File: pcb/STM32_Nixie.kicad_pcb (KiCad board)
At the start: 2 copper layers, 134 parts, among them J1 CONN_USBC_RCPT_USB2.0_USB4085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, J1 CON_SAMTEC_14P_2R_1m27_P_KEY_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, J2 CONN_USBC_RCPT_USB2.0_USB4085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, Q1 NFET_250V_10A_TPH1110FNH,L1Q, SW1 ENC_SPST_24PPR_PEC12R-4225F-S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, U1 IC_HV5622PG-G, U2 IC_HV5622PG-G, U3 IC_MCU_STM32F100C4T6B_48LQFP, U4 IC_LVL_MC14504BDTR2G, U5 REG_SW_BOOST_TI_TLV61046ADBV, U6 REG_SW_BOOST_TI_LM51561HPWPR, U7 REG_LDO_3V3_250mA_TI_LP5907MF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, U8 IC_FTDI_FT231XS, X1 XTAL_8M_20PPM_18pF_ECS-80-18-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, X2 XTAL_32K768_10PPM_7pF_ECS-.32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

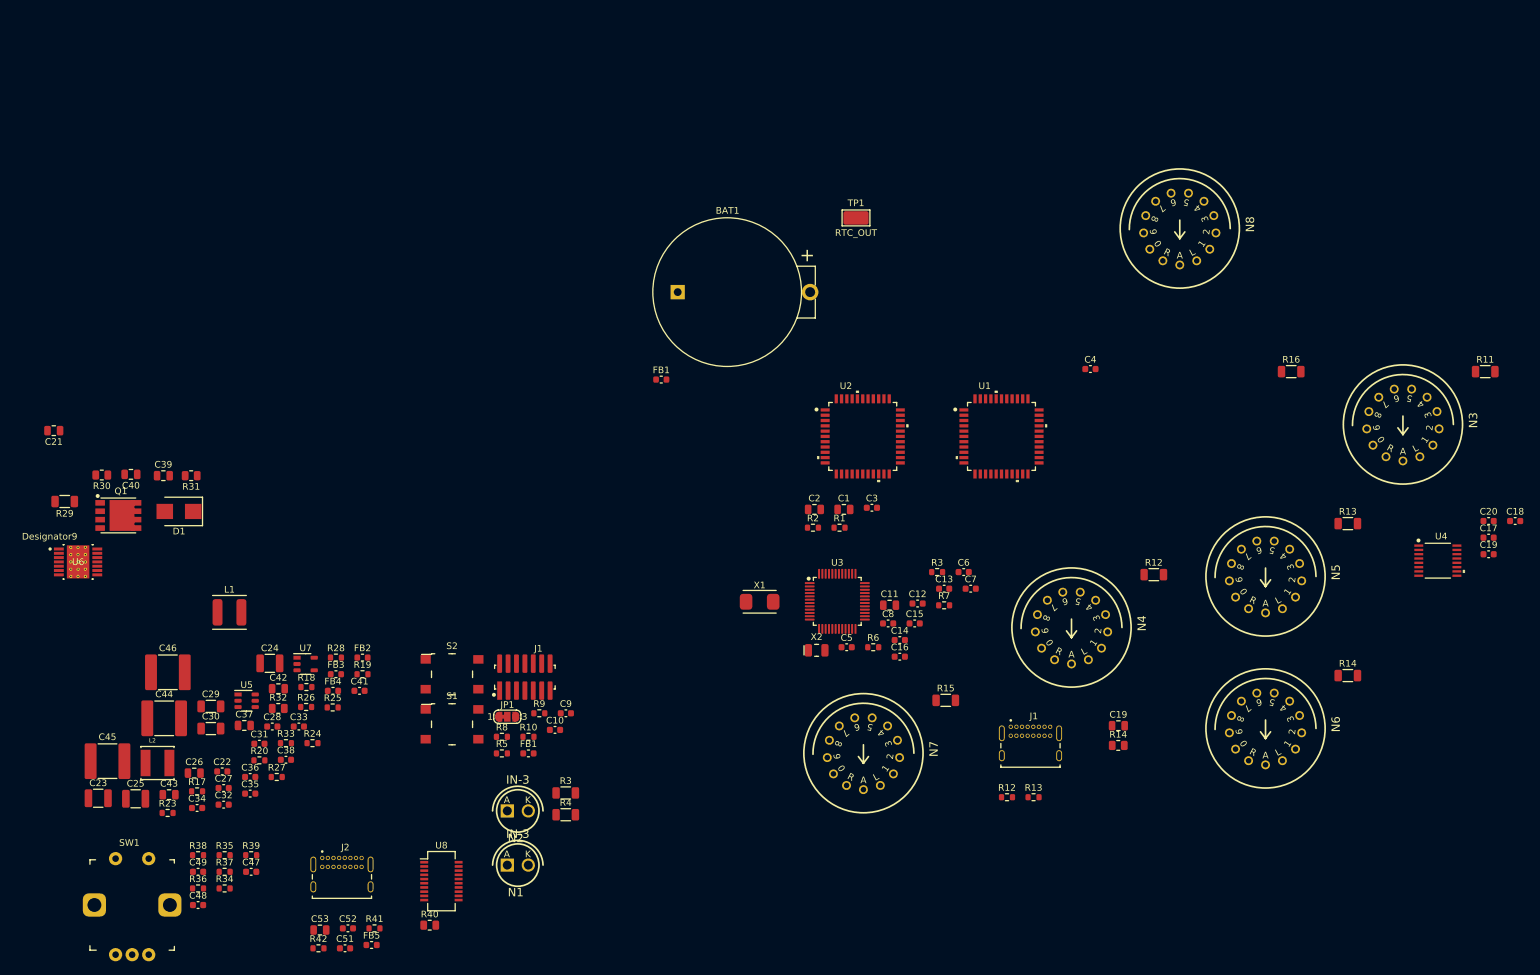
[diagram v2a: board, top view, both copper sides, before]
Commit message: Fixed a bunch of footprints and added missing 3D models
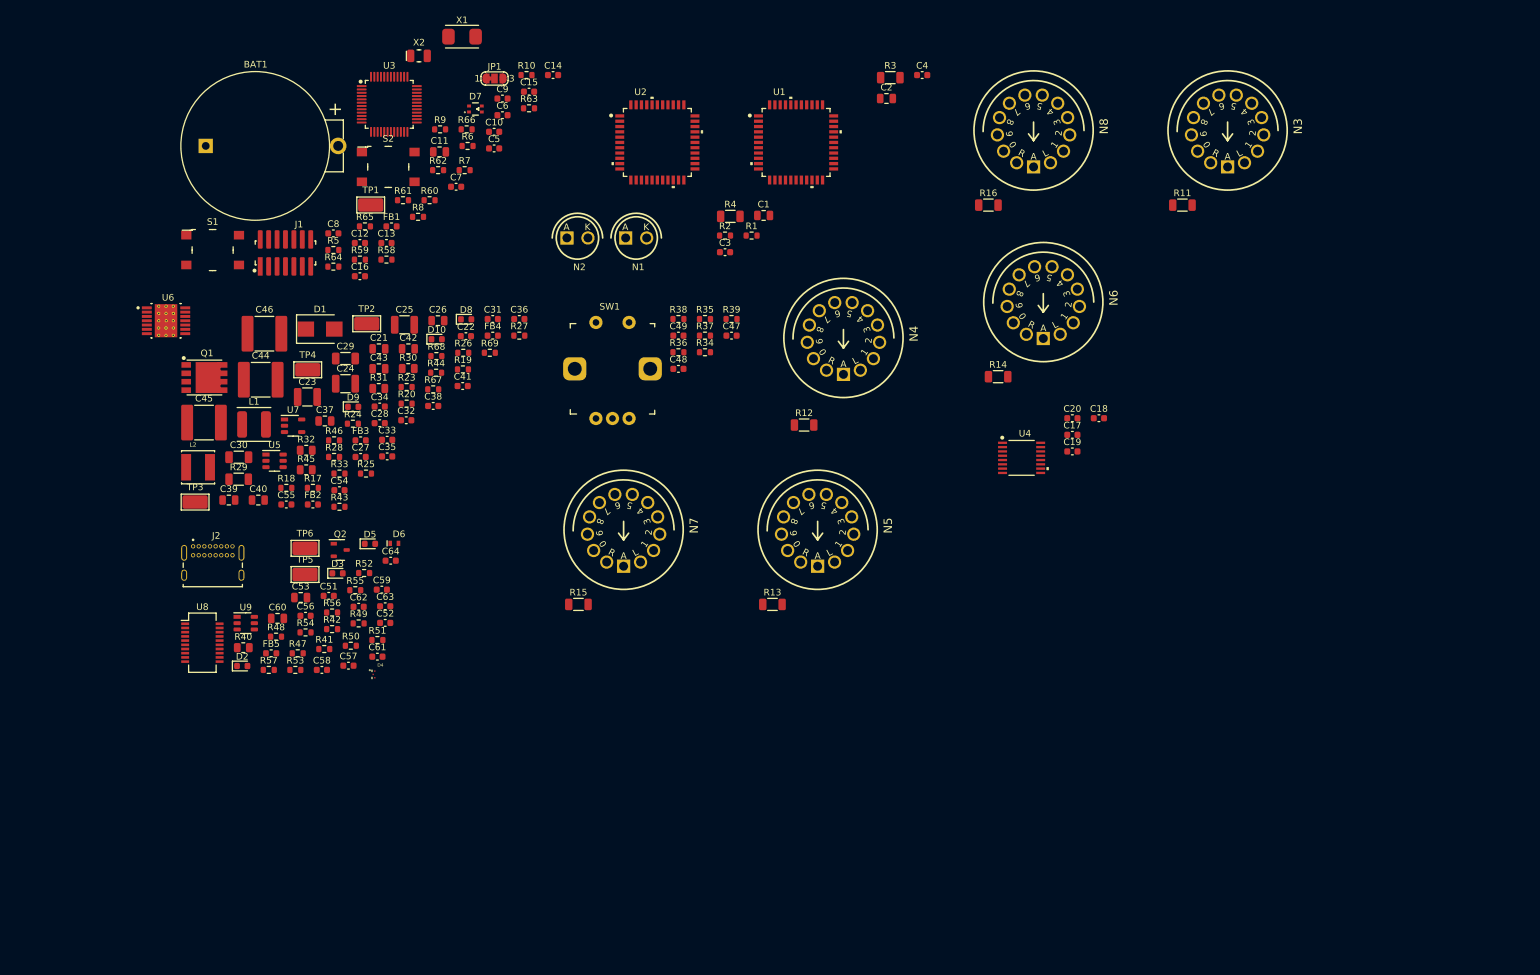
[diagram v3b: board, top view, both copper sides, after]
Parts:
- removed the C19 at (233.3, 95.4)
- removed the C19 at (177.4, 121.3)
- removed the FB1 at (108.4, 69.0)
- removed the FB1 at (88.3, 125.4)
- removed the J1 at (164.1, 125.8)
- removed the J1 at (87.8, 113.9)
- removed the R12 at (160.6, 132.1)
- removed the R12 at (182.8, 98.4)
- removed the R13 at (164.6, 132.1)
- removed the R13 at (212.1, 90.7)
- removed the R14 at (212.1, 113.7)
- removed the R14 at (177.4, 124.2)
- removed the R3 at (94.0, 131.4)
- removed the R3 at (150.0, 98.1)
- added C19: CAP_CER_0u1_50V_X7R_0603, Capacitor_SMD:C_0603_1608Metric, F.Cu at (170.5, 79.8)
- added C54: CAP_CER_0u1_50V_X7R_0603, Capacitor_SMD:C_0603_1608Metric, F.Cu at (59.8, 85.7)
- added C55: CAP_CER_0u1_50V_X7R_0603, Capacitor_SMD:C_0603_1608Metric, F.Cu at (51.8, 87.8)
- added C56: CAP_CER_47p_50V_NP0_0603, Capacitor_SMD:C_0603_1608Metric, F.Cu at (54.7, 104.7)
- added C57: CAP_CER_47p_50V_NP0_0603, Capacitor_SMD:C_0603_1608Metric, F.Cu at (61.1, 112.2)
- added C58: CAP_CER_0u1_50V_X7R_0603, Capacitor_SMD:C_0603_1608Metric, F.Cu at (57.1, 112.8)
- added C59: CAP_CER_0u1_50V_X7R_0603, Capacitor_SMD:C_0603_1608Metric, F.Cu at (66.2, 100.7)
- added C60: CAP_CER_4u7_16V_X7R_0805, Capacitor_SMD:C_0805_2012Metric, F.Cu at (50.4, 105.0)
- added C61: CAP_CER_0u1_50V_X7R_0603, Capacitor_SMD:C_0603_1608Metric, F.Cu at (65.5, 110.8)
- added C62: CAP_CER_0u1_50V_X7R_0603, Capacitor_SMD:C_0603_1608Metric, F.Cu at (62.7, 103.3)
- added C63: CAP_CER_0u1_50V_X7R_0603, Capacitor_SMD:C_0603_1608Metric, F.Cu at (66.7, 103.2)
- added C64: CAP_CER_0u1_50V_X7R_0603, Capacitor_SMD:C_0603_1608Metric, F.Cu at (67.5, 96.3)
- added D10: LED_GREEN_0603, LED_SMD:LED_0603_1608Metric, F.Cu at (74.5, 62.9)
- added D2: LED_AMBER_0603, LED_SMD:LED_0603_1608Metric, F.Cu at (45.1, 112.2)
- added D3: LED_GREEN_0603, LED_SMD:LED_0603_1608Metric, F.Cu at (59.5, 98.2)
- added D4: D_TVS_BI_3V6_20W_3-XFDFN, arjun_footprints:DIO_ESD122DMYR, F.Cu at (65.0, 113.5)
- added D5: LED_RED_0603, LED_SMD:LED_0603_1608Metric, F.Cu at (64.4, 93.8)
- added D6: D_TVS_UNI_5V_700W_2-UDFN, arjun_footprints:QFN-2L_STM, F.Cu at (68.1, 93.7)
- added D7: LED_RGB_0606, arjun_footprints:EAST1616RGBB2_EVE, F.Cu at (80.3, 28.1)
- added D8: LED_AMBER_0603, LED_SMD:LED_0603_1608Metric, F.Cu at (78.9, 59.9)
- added D9: LED_GREEN_0603, LED_SMD:LED_0603_1608Metric, F.Cu at (61.9, 73.1)
- added FB1: FER_1K_0A6_0603, Inductor_SMD:L_0603_1608Metric, F.Cu at (67.6, 45.9)
- added J1: CON_SAMTEC_14P_2R_1m27_P_KEY_FTSH-107-01-L-DV-K-TR, arjun_footprints:CON_FTSH-107-01-x-DV-K, F.Cu at (51.6, 49.9)
- added Q2: NFET_60V_0A5_2N7002KT1G, arjun_footprints:SOT-23_ONSEMI, F.Cu at (59.9, 94.7)
- added R12: RES_17K4_1P_1/4W_1206, Resistor_SMD:R_1206_3216Metric, F.Cu at (130.0, 75.8)
- added R13: RES_17K4_1P_1/4W_1206, Resistor_SMD:R_1206_3216Metric, F.Cu at (125.2, 102.9)
- added R14: RES_17K4_1P_1/4W_1206, Resistor_SMD:R_1206_3216Metric, F.Cu at (159.3, 68.5)
- added R3: RES_150K_1P_1/4W_1206, Resistor_SMD:R_1206_3216Metric, F.Cu at (143.0, 23.4)
- added R43: RES_33K_1P_1/10W_0603, Resistor_SMD:R_0603_1608Metric, F.Cu at (59.8, 88.2)
- added R44: RES_4K7_1P_1/10W_0603, Resistor_SMD:R_0603_1608Metric, F.Cu at (74.4, 68.0)
- added R45: RES_499K_1P_1/4W_0805, Resistor_SMD:R_0805_2012Metric, F.Cu at (54.8, 82.6)
- added R46: RES_4K7_1P_1/10W_0603, Resistor_SMD:R_0603_1608Metric, F.Cu at (59.0, 78.2)
- added R47: RES_27R_1P_1/10W_0603, Resistor_SMD:R_0603_1608Metric, F.Cu at (53.5, 110.3)
- added R48: RES_27R_1P_1/10W_0603, Resistor_SMD:R_0603_1608Metric, F.Cu at (50.2, 107.8)
- added R49: RES_10K_1P_1/10W_0603, Resistor_SMD:R_0603_1608Metric, F.Cu at (62.7, 105.8)
- added R50: RES_1K5_1P_1/10W_0603, Resistor_SMD:R_0603_1608Metric, F.Cu at (61.5, 109.2)
- added R51: RES_698R_1P_1/10W_0603, Resistor_SMD:R_0603_1608Metric, F.Cu at (65.5, 108.3)
- added R52: RES_DNP_0603, Resistor_SMD:R_0603_1608Metric, F.Cu at (63.5, 98.2)
- added R53: RES_10K_1P_1/10W_0603, Resistor_SMD:R_0603_1608Metric, F.Cu at (53.1, 112.8)
- added R54: RES_232K_1P_1/10W_0603, Resistor_SMD:R_0603_1608Metric, F.Cu at (54.7, 107.2)
- added R55: RES_26K1_1P_1/10W_0603, Resistor_SMD:R_0603_1608Metric, F.Cu at (62.2, 100.8)
- added R56: RES_10K_1P_1/10W_0603, Resistor_SMD:R_0603_1608Metric, F.Cu at (58.7, 104.2)
- added R57: RES_3K3_1P_1/10W_0603, Resistor_SMD:R_0603_1608Metric, F.Cu at (49.1, 112.8)
- added R58: RES_499R_1P_1/10W_0603, Resistor_SMD:R_0603_1608Metric, F.Cu at (66.9, 50.9)
- added R59: RES_1K5_1P_1/10W_0603, Resistor_SMD:R_0603_1608Metric, F.Cu at (62.9, 50.9)
- added R60: RES_698R_1P_1/10W_0603, Resistor_SMD:R_0603_1608Metric, F.Cu at (73.4, 41.9)
- added R61: RES_10K_1P_1/10W_0603, Resistor_SMD:R_0603_1608Metric, F.Cu at (69.4, 41.9)
- added R62: RES_10K_1P_1/10W_0603, Resistor_SMD:R_0603_1608Metric, F.Cu at (74.7, 37.4)
- added R63: RES_10K_1P_1/10W_0603, Resistor_SMD:R_0603_1608Metric, F.Cu at (88.4, 28.0)
- added R64: RES_30R_1P_1/10W_0603, Resistor_SMD:R_0603_1608Metric, F.Cu at (58.9, 51.9)
- added R65: RES_30R_1P_1/10W_0603, Resistor_SMD:R_0603_1608Metric, F.Cu at (63.6, 45.9)
- added R66: RES_30R_1P_1/10W_0603, Resistor_SMD:R_0603_1608Metric, F.Cu at (79.0, 31.2)
- added R67: RES_1K5_1P_1/10W_0603, Resistor_SMD:R_0603_1608Metric, F.Cu at (73.9, 70.5)
- added R68: RES_9K31_1P_1/10W_0603, Resistor_SMD:R_0603_1608Metric, F.Cu at (74.4, 65.4)
- added R69: RES_698R_1P_1/10W_0603, Resistor_SMD:R_0603_1608Metric, F.Cu at (82.5, 64.9)
- added TP2: TP_KEYSTONE_5019, arjun_footprints:TestPoint_Keystone_5019_Minature, F.Cu at (63.9, 60.6)
- added TP3: TP_KEYSTONE_5019, arjun_footprints:TestPoint_Keystone_5019_Minature, F.Cu at (38.0, 87.5)
- added TP4: TP_KEYSTONE_5019, arjun_footprints:TestPoint_Keystone_5019_Minature, F.Cu at (55.0, 67.5)
- added TP5: TP_KEYSTONE_5019, arjun_footprints:TestPoint_Keystone_5019_Minature, F.Cu at (54.6, 98.4)
- added TP6: TP_KEYSTONE_5019, arjun_footprints:TestPoint_Keystone_5019_Minature, F.Cu at (54.6, 94.5)
- added U9: IC_LSW_TI_TPS2552D, arjun_footprints:SOT-23-6_TI, F.Cu at (45.6, 105.8)
- N1, N2: value IN-3 -> Val**
- N3, N4, N5, N6, N7, N8: value IN-14 -> Val**
- U1, U2: value IC_HV5622PG-G -> IC_SR_MC_HV5622PG-G
- U4: value IC_LVL_MC14504BDTR2G -> IC_LVL_ONSEMI_MC14504BDTR2G
- moved R34 108.7 mm to (115.0, 64.9)
- moved R36 108.7 mm to (111.0, 64.9)
- moved SW1 108.7 mm to (95.3, 67.4)
- moved C47 108.7 mm to (119.0, 62.4)
- moved C48 108.7 mm to (111.0, 67.4)
- moved C49 108.7 mm to (111.0, 62.4)
- moved R35 108.7 mm to (115.0, 59.8)
- moved R37 108.7 mm to (115.0, 62.4)
- moved R38 108.7 mm to (111.0, 59.8)
- moved R39 108.7 mm to (119.0, 59.8)
- moved X2 108.0 mm to (71.8, 20.1)
- moved C8 102.4 mm to (58.9, 46.9)
- moved U3 101.0 mm to (67.3, 27.4)
- moved C12 100.3 mm to (62.9, 48.4)
- moved C14 100.1 mm to (92.0, 23.0)
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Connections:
- C51 pad 1: /USB Connector/USB_VBUS -> /USB Connector/USB_VBUS_FB
- C52 pad 1: +5V -> /USB Connector/USB_VBUS
- C53 pad 1: +5V -> /USB Connector/USB_VBUS
- FB5 pad 1: /USB Connector/USB_VBUS -> /USB Connector/USB_VBUS_FB
- FB5 pad 2: +5V -> /USB Connector/USB_VBUS
- J2 pad A4: /USB Connector/USB_VBUS -> /USB Connector/USB_VBUS_FB
- J2 pad A9: /USB Connector/USB_VBUS -> /USB Connector/USB_VBUS_FB
- J2 pad B4: /USB Connector/USB_VBUS -> /USB Connector/USB_VBUS_FB
- J2 pad B9: /USB Connector/USB_VBUS -> /USB Connector/USB_VBUS_FB
- R17 pad 1: /Power/EN_12V -> /MCU/EN_12V
- R19 pad 1: /Power/EN_180V -> /MCU/EN_180V
- R20 pad 2: /Power/PGOOD_180V -> /MCU/PG_180V
- R23 pad 1: /Power/DITHOFF -> /MCU/DITHOFF_180V
- U3 pad 14: /SPI_nCS_nLE_3V3 -> /MCU/SPI_nCS_nLE_R
- U3 pad 15: /SPI_SCK_3V3 -> /MCU/SPI_SCK_R
- U3 pad 17: /SPI_PICO_3V3 -> /MCU/SPI_PICO_R
- U3 pad 18: unconnected-(U3-Pad18) -> /MCU/SENSE_12V
- U3 pad 19: /MCU/HV_MON_BUF -> /MCU/SENSE_180V
- U3 pad 21: unconnected-(U3-Pad21) -> /MCU/PG_180V
- U3 pad 22: unconnected-(U3-Pad22) -> /MCU/DITHOFF_180V
- U3 pad 25: /MCU/HV_EN -> /MCU/EN_180V
- U3 pad 28: unconnected-(U3-Pad28) -> /MCU/EN_12V
- U3 pad 38: unconnected-(U3-Pad38) -> /MCU/LED_GREEN
- U3 pad 40: unconnected-(U3-Pad40) -> /MCU/LED_RED
- U3 pad 41: unconnected-(U3-Pad41) -> /MCU/LED_BLUE
- U3 pad 42: unconnected-(U3-Pad42) -> /MCU/SET_ILIM
- U3 pad 43: unconnected-(U3-Pad43) -> /MCU/HW_REV2
- U3 pad 45: unconnected-(U3-Pad45) -> /MCU/HW_REV1
- U3 pad 46: unconnected-(U3-Pad46) -> /MCU/HW_REV0
- U5 pad 4: /Power/EN_12V -> /MCU/EN_12V
- U6 pad 13: /Power/PGOOD_180V -> /MCU/PG_180V
- U6 pad 14: /Power/EN_180V -> /MCU/EN_180V
- U6 pad 9: /Power/DITHOFF -> /MCU/DITHOFF_180V
- U8 pad 10: unconnected-(U8-Pad10) -> /USB Connector/nTXLED
- U8 pad 11: unconnected-(U8-Pad11) -> /USB Connector/USB_D_R_P
- U8 pad 12: unconnected-(U8-Pad12) -> /USB Connector/USB_D_R_N
- U8 pad 13: unconnected-(U8-Pad13) -> +3.3V
- U8 pad 14: unconnected-(U8-Pad14) -> /USB Connector/nFTDI_RESET
- U8 pad 15: unconnected-(U8-Pad15) -> +3.3V
- U8 pad 16: unconnected-(U8-Pad16) -> GND
- U8 pad 17: unconnected-(U8-Pad17) -> /USB Connector/nRXLED
- U8 pad 20: unconnected-(U8-Pad20) -> /MCU/UART_BL_RX
- U8 pad 3: unconnected-(U8-Pad3) -> +3.3V
- U8 pad 4: unconnected-(U8-Pad4) -> /MCU/UART_BL_TX
- U8 pad 6: unconnected-(U8-Pad6) -> GND

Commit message: Started layout!! 180V boost mostly laid out
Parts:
- added C50: CAP_CER_4700p_250V_X7R_0805, Capacitor_SMD:C_0805_2012Metric, F.Cu at (1.73, 8.03)
- added R21: RES_1M_1P_1/10W_0603, Resistor_SMD:R_0603_1608Metric, F.Cu at (1.50, 0.76)
- added R22: RES_71K5_1P_1/10W_0603, Resistor_SMD:R_0603_1608Metric, F.Cu at (1.50, 3.27)
- N1, N2: value Val** -> IN-3
- N3, N4, N5, N6, N7, N8: value Val** -> IN-14
- moved C29 193.2 mm to (245.6, 121.9)
- moved C38 193.2 mm to (258.9, 129.1)
- moved C42 193.2 mm to (255.1, 120.4)
- moved D9 193.2 mm to (246.8, 129.2)
- moved FB4 193.2 mm to (267.9, 118.4)
- moved L1 193.2 mm to (231.8, 131.8)
- moved R67 193.2 mm to (258.9, 126.5)
- moved R69 193.2 mm to (267.4, 121.0)
- moved C21 193.2 mm to (250.7, 120.4)
- moved C22 193.2 mm to (263.8, 118.5)
- moved C28 193.2 mm to (250.8, 131.7)
- moved C30 193.2 mm to (229.5, 136.8)
- moved C37 193.2 mm to (242.5, 131.3)
- moved C41 193.2 mm to (263.3, 126.0)
- moved C54 193.2 mm to (244.7, 141.8)
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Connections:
- BAT1 pad Pos: 180V -> +3.3VBAT
- U3 pad 1: 180V -> +3.3VBAT
- U6 pad 15: unconnected-(U6-Pad15) -> GND
- U6 pad 5: unconnected-(U6-Pad5) -> GND
- U6 pad 6: unconnected-(U6-Pad6) -> GND
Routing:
- net 180V: track 0.00 -> 35.6 mm, vias 0 -> 2
- net /Power/GATE_R: track 0.00 -> 15.0 mm, vias 0 -> 2
- net /Power/FB_180V: track 0.00 -> 11.4 mm, vias 0 -> 2
- net /Power/CS_RAW: track 0.00 -> 8.89 mm, vias 0 -> 2
- net /MCU/DITHOFF_180V: track 0.00 -> 7.67 mm, vias 0 -> 2
- net /MCU/PG_180V: track 0.00 -> 7.27 mm
- net GND: track 0.00 -> 6.71 mm, vias 0 -> 12
- net /Power/RT_180V: track 0.00 -> 5.78 mm
- net /Power/SS_180V: track 0.00 -> 5.44 mm
- net /MCU/EN_180V: track 0.00 -> 1.93 mm
- added copper zone on F.Cu, net GND
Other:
- copper layers 2 -> 4
- rule pad_to_mask_clearance: 0 -> 0.038
